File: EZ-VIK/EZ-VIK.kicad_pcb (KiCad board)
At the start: 2 copper layers, 12.7 x 10.3 mm, 4 parts, among them J1 Conn_01x04, J2 Conn_01x04, J3 Conn_01x04

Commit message: Initial update
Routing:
- net SCLK: track 8.10 -> 7.11 mm
- net MISO: track 6.59 -> 6.04 mm
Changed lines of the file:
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@@
   (gr_line (start 158.750116 111.33) (end 158.750116 101.87)
     (stroke (width 0.1) (type default)) (layer "Edge.Cuts"))
-  (segment (start 148.65 102.86) (end 146.05 102.86) (width 0.25) (layer "F.Cu") (net 1))
-  (segment (start 149.65 103.86) (end 148.65 102.86) (width 0.25) (layer "F.Cu") (net 1))
-  (segment (start 149.65 107.95) (end 149.65 103.86) (width 0.25) (layer "F.Cu") (net 1))
+  (segment (start 147.16 102.86) (end 146.174884 102.86) (width 0.25) (layer "F.Cu") (net 1))
+  (segment (start 148.25 103.95) (end 147.16 102.86) (width 0.25) (layer "F.Cu") (net 1))
+  (segment (start 148.25 106.55) (end 148.25 103.95) (width 0.25) (layer "F.Cu") (net 1))
+  (segment (start 149.65 107.95) (end 148.25 106.55) (width 0.25) (layer "F.Cu") (net 1))
+  (segment (start 150.125 108.6) (end 149.175 108.6) (width 0.25) (layer "F.Cu") (net 2))
+  (segment (start 149.175 108.6) (end 146.174884 105.599884) (width 0.25) (layer "F.Cu") (net 2))
+  (segment (start 146.174884 105.599884) (end 146.174884 105.41) (width 0.25) (layer "F.Cu") (net 2))
+  (segment (start 150.15 107.95) (end 150.15 108.575) (width 0.25) (layer "F.Cu") (net 2))
   (segment (start 150.15 108.575) (end 150.125 108.6) (width 0.25) (layer "F.Cu") (net 2))
-  (segment (start 149.175 107.685) (end 146.9 105.41) (width 0.25) (layer "F.Cu") (net 2))
-  (segment (start 146.9 105.41) (end 146.05 105.41) (width 0.25) (layer "F.Cu") (net 2))
-  (segment (start 150.125 108.6) (end 149.175 108.6) (width 0.25) (layer "F.Cu") (net 2))
-  (segment (start 150.15 107.95) (end 150.15 108.575) (width 0.25) (layer "F.Cu") (net 2))
-  (segment (start 149.175 108.6) (end 149.175 107.685) (width 0.25) (layer "F.Cu") (net 2))
   (segment (start 150.65 107.95) (end 150.65 108.711396) (width 0.25) (layer "F.Cu") (net 3))
   (segment (start 150.65 108.711396) (end 150.311396 109.05) (width 0.25) (layer "F.Cu") (net 3))
@@
   (segment (start 147.908604 107.97) (end 146.075 107.97) (width 0.25) (layer "F.Cu") (net 3))
   (segment (start 146.075 107.97) (end 146.05 107.945) (width 0.25) (layer "F.Cu") (net 3))
+  (segment (start 151.15 107.95) (end 151.15 108.847792) (width 0.25) (layer "F.Cu") (net 4))
   (segment (start 151.15 108.847792) (end 150.497792 109.5) (width 0.25) (layer "F.Cu") (net 4))
-  (segment (start 147.95 108.99) (end 146.46 110.48) (width 0.25) (layer "F.Cu") (net 4))
-  (segment (start 151.15 107.95) (end 151.15 108.847792) (width 0.25) (layer "F.Cu") (net 4))
-  (segment (start 148.802208 109.5) (end 148.292208 108.99) (width 0.25) (layer "F.Cu") (net 4))
-  (segment (start 150.497792 109.5) (end 148.802208 109.5) (width 0.25) (layer "F.Cu") (net 4))
+  (segment (start 148.25 109.5) (end 147.27 110.48) (width 0.25) (layer "F.Cu") (net 4))
+  (segment (start 150.497792 109.5) (end 148.25 109.5) (width 0.25) (layer "F.Cu") (net 4))
   (segment (start 146.46 110.48) (end 146.05 110.48) (width 0.25) (layer "F.Cu") (net 4))
-  (segment (start 148.292208 108.99) (end 147.95 108.99) (width 0.25) (layer "F.Cu") (net 4))
-  (segment (start 148.585 110.885) (end 148.585 111.76) (width 0.25) (layer "F.Cu") (net 5))
-  (segment (start 149.52 109.95) (end 148.585 110.885) (width 0.25) (layer "F.Cu") (net 5))
+  (segment (start 147.27 110.48) (end 146.174884 110.48) (width 0.25) (layer "F.Cu") (net 4))
+  (segment (start 150.684188 109.95) (end 149.45 109.95) (width 0.25) (layer "F.Cu") (net 5))
+  (segment (start 148.585 110.815) (end 148.585 111.635116) (width 0.25) (layer "F.Cu") (net 5))
+  (segment (start 151.65 107.95) (end 151.65 108.984188) (width 0.25) (layer "F.Cu") (net 5))
+  (segment (start 149.45 109.95) (end 148.585 110.815) (width 0.25) (layer "F.Cu") (net 5))
   (segment (start 151.65 108.984188) (end 150.684188 109.95) (width 0.25) (layer "F.Cu") (net 5))
-  (segment (start 151.65 107.95) (end 151.65 108.984188) (width 0.25) (layer "F.Cu") (net 5))
-  (segment (start 150.684188 109.95) (end 149.52 109.95) (width 0.25) (layer "F.Cu") (net 5))
   (segment (start 152.15 109.39) (end 151.135 110.405) (width 0.25) (layer "F.Cu") (net 6))
   (segment (start 151.135 110.405) (end 151.135 111.76) (width 0.25) (layer "F.Cu") (net 6))

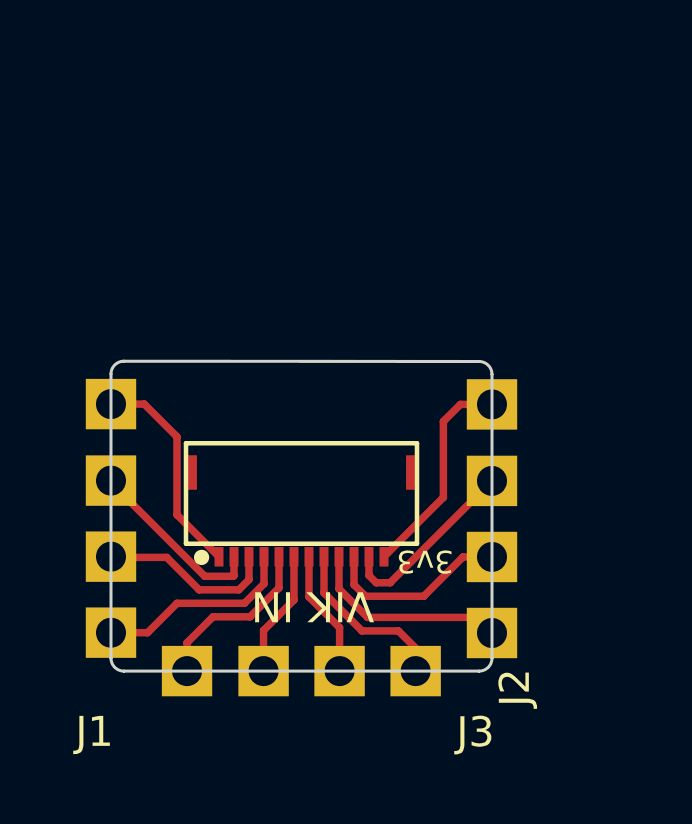
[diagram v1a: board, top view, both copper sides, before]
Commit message: Split into full size and mini
Added Mini branch, and changed main branch to the full size VIK connector.
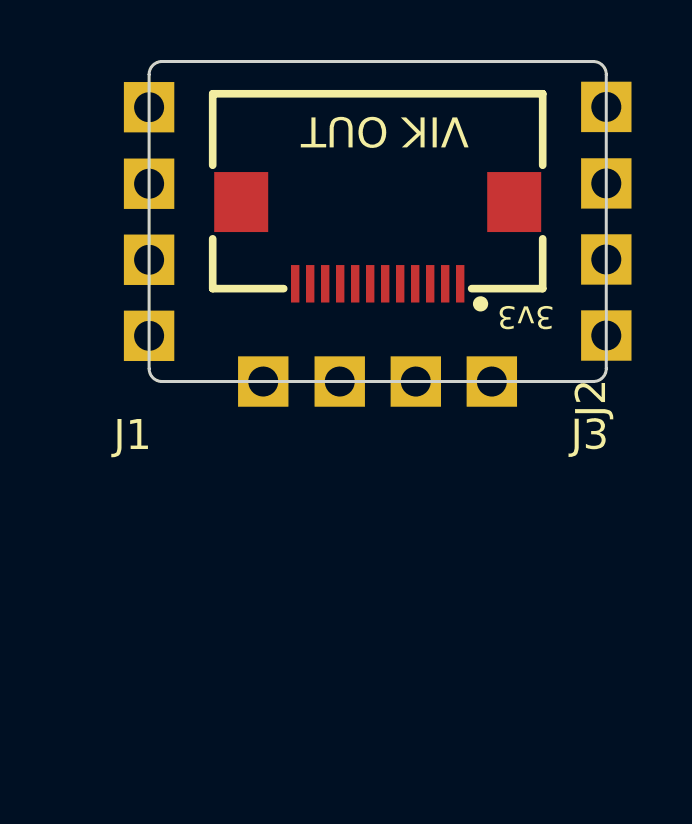
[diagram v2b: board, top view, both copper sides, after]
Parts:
- J4: footprint vik:vik-keyboard-connector-horizontal-mini -> vik:vik-keyboard-connector-horizontal
- moved J3 10.6 mm to (162.0, 104.4)
- moved J2 9.98 mm to (162.6, 102.7)
- moved J1 9.98 mm to (146.8, 104.4)
- moved J4 9.38 mm to (154.9, 96.8)
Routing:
- net +3V3: track 7.19 -> 0.00 mm
- net SCLK: track 7.11 -> 0.00 mm
- net GP_AD2: track 6.96 -> 0.00 mm
- net SCL: track 6.78 -> 0.00 mm
- net SDA: track 6.23 -> 0.00 mm
- net GND: track 6.23 -> 0.00 mm
- net MISO: track 6.04 -> 0.00 mm
- net SPI_CS: track 5.96 -> 0.00 mm
- net RGB_DO: track 5.79 -> 0.00 mm
- net MOSI: track 5.68 -> 0.00 mm
- net +5V: track 4.23 -> 0.00 mm
- net GP_AD1: track 4.23 -> 0.00 mm
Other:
- board size 12.7 x 10.3 mm -> 15.2 x 10.7 mm

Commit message: Finished tracework.
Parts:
- moved J4 0.42 mm to (154.9, 96.4)
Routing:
- net +3V3: track 0.00 -> 9.05 mm
- net SCLK: track 0.00 -> 9.04 mm
- net GND: track 0.00 -> 8.04 mm
- net GP_AD2: track 0.00 -> 7.91 mm
- net SCL: track 0.00 -> 7.90 mm
- net MISO: track 0.00 -> 7.90 mm
- net SDA: track 0.00 -> 7.76 mm
- net SPI_CS: track 0.00 -> 7.73 mm
- net MOSI: track 0.00 -> 5.31 mm
- net RGB_DO: track 0.00 -> 5.30 mm
- net +5V: track 0.00 -> 3.97 mm
- net GP_AD1: track 0.00 -> 3.97 mm
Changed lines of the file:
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@@
     (property "ki_keywords" "connector")
     (attr smd)
-    (fp_text reference "J2" (at 0 -0.5 90 unlocked) (layer "F.SilkS")
+    (fp_text reference "J2" (at -0.466 -0.4522 90 unlocked) (layer "F.SilkS")
         (effects (font (size 1 1) (thickness 0.1)))
     )
@@
   )
   (footprint "vik:vik-keyboard-connector-horizontal" (layer "F.Cu")
-    (at 154.94 96.811 180)
+    (at 154.94 96.393 180)
     (property "Sheetfile" "EZ-VIK.kicad_sch")
     (property "Sheetname" "")
@@
   (gr_line (start 162.558978 101.676862) (end 162.558978 91.871138)
     (stroke (width 0.1) (type default)) (layer "Edge.Cuts"))
+  (segment (start 150.197 92.964) (end 147.445114 92.964) (width 0.25) (layer "F.Cu") (net 1))
+  (segment (start 152.19 94.957) (end 150.197 92.964) (width 0.25) (layer "F.Cu") (net 1))
+  (segment (start 152.19 98.431) (end 152.19 94.957) (width 0.25) (layer "F.Cu") (net 1))
+  (segment (start 152.595 99.441) (end 151.247 99.441) (width 0.25) (layer "F.Cu") (net 2))
+  (segment (start 152.69 98.431) (end 152.69 99.346) (width 0.25) (layer "F.Cu") (net 2))
+  (segment (start 151.247 99.441) (end 147.445393 95.639393) (width 0.25) (layer "F.Cu") (net 2))
+  (segment (start 147.445393 95.639393) (end 147.44538 95.513987) (width 0.25) (layer "F.Cu") (net 2))
+  (segment (start 152.69 99.346) (end 152.595 99.441) (width 0.25) (layer "F.Cu") (net 2))
+  (segment (start 153.19 99.482396) (end 152.781396 99.891) (width 0.25) (layer "F.Cu") (net 3))
+  (segment (start 149.287644 99.891) (end 147.445644 98.049) (width 0.25) (layer "F.Cu") (net 3))
+  (segment (start 152.781396 99.891) (end 149.287644 99.891) (width 0.25) (layer "F.Cu") (net 3))
+  (segment (start 153.19 98.431) (end 153.19 99.482396) (width 0.25) (layer "F.Cu") (net 3))
+  (segment (start 147.445895 100.458105) (end 147.445908 100.583987) (width 0.25) (layer "F.Cu") (net 4))
+  (segment (start 153.69 99.618792) (end 152.967792 100.341) (width 0.25) (layer "F.Cu") (net 4))
+  (segment (start 147.563 100.341) (end 147.445895 100.458105) (width 0.25) (layer "F.Cu") (net 4))
+  (segment (start 153.69 98.431) (end 153.69 99.618792) (width 0.25) (layer "F.Cu") (net 4))
+  (segment (start 152.967792 100.341) (end 147.563 100.341) (width 0.25) (layer "F.Cu") (net 4))
+  (segment (start 154.19 99.755188) (end 153.002188 100.943) (width 0.25) (layer "F.Cu") (net 5))
+  (segment (start 154.19 98.431) (end 154.19 99.755188) (width 0.25) (layer "F.Cu") (net 5))
+  (segment (start 153.002188 100.943) (end 152.163978 100.943) (width 0.25) (layer "F.Cu") (net 5))
+  (segment (start 152.163978 100.943) (end 151.125 101.981978) (width 0.25) (layer "F.Cu") (net 5))
+  (segment (start 154.69 100.966978) (end 153.675 101.981978) (width 0.25) (layer "F.Cu") (net 6))
+  (segment (start 154.69 98.431) (end 154.69 100.966978) (width 0.25) (layer "F.Cu") (net 6))
+  (segment (start 155.19 98.431) (end 155.19 100.961978) (width 0.25) (layer "F.Cu") (net 7))
+  (segment (start 155.19 100.961978) (end 156.21 101.981978) (width 0.25) (layer "F.Cu") (net 7))
+  (segment (start 157.706022 100.943) (end 158.745 101.981978) (width 0.25) (layer "F.Cu") (net 8))
+  (segment (start 155.69 99.755188) (end 156.877812 100.943) (width 0.25) (layer "F.Cu") (net 8))
+  (segment (start 156.877812 100.943) (end 157.706022 100.943) (width 0.25) (layer "F.Cu") (net 8))
+  (segment (start 155.69 98.431) (end 155.69 99.755188) (width 0.25) (layer "F.Cu") (net 8))
+  (segment (start 157.69 94.957) (end 159.693 92.954) (width 0.25) (layer "F.Cu") (net 9))
+  (segment (start 159.693 92.954) (end 162.433978 92.954) (width 0.25) (layer "F.Cu") (net 9))
+  (segment (start 157.69 98.431) (end 157.69 94.957) (width 0.25) (layer "F.Cu") (net 9))
+  (segment (start 162.433978 95.835022) (end 162.433978 95.504) (width 0.25) (layer "F.Cu") (net 10))
+  (segment (start 157.19 98.431) (end 157.19 99.346) (width 0.25) (layer "F.Cu") (net 10))
+  (segment (start 158.8026 99.4664) (end 162.433978 95.835022) (width 0.25) (layer "F.Cu") (net 10))
+  (segment (start 157.3104 99.4664) (end 158.8026 99.4664) (width 0.25) (layer "F.Cu") (net 10))
+  (segment (start 157.19 99.346) (end 157.3104 99.4664) (width 0.25) (layer "F.Cu") (net 10))
+  (segment (start 156.69 98.431) (end 156.69 99.482396) (width 0.25) (layer "F.Cu") (net 11))
+  (segment (start 157.131204 99.9236) (end 160.549378 99.9236) (width 0.25) (layer "F.Cu") (net 11))
+  (segment (start 156.69 99.482396) (end 157.131204 99.9236) (width 0.25) (layer "F.Cu") (net 11))
+  (segment (start 160.549378 99.9236) (end 162.433978 98.039) (width 0.25) (layer "F.Cu") (net 11))
+  (segment (start 156.19 99.618792) (end 156.944808 100.3736) (width 0.25) (layer "F.Cu") (net 12))
+  (segment (start 156.19 98.431) (end 156.19 99.618792) (width 0.25) (layer "F.Cu") (net 12))
+  (segment (start 156.944808 100.3736) (end 162.3596 100.3736) (width 0.25) (layer "F.Cu") (net 12))
+  (segment (start 162.3596 100.3736) (end 162.433978 100.447978) (width 0.25) (layer "F.Cu") (net 12))
+  (segment (start 162.433978 100.447978) (end 162.433978 100.574) (width 0.25) (layer "F.Cu") (net 12))
 )
